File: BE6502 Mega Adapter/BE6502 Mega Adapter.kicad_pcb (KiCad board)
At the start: 2 copper layers, 99.1 x 99.1 mm, 12 parts, among them J1 Expansion, J2 Slot #1, J3 Slot #2, M1 Mounting, M2 Mounting, M3 Mounting, M4 Mounting

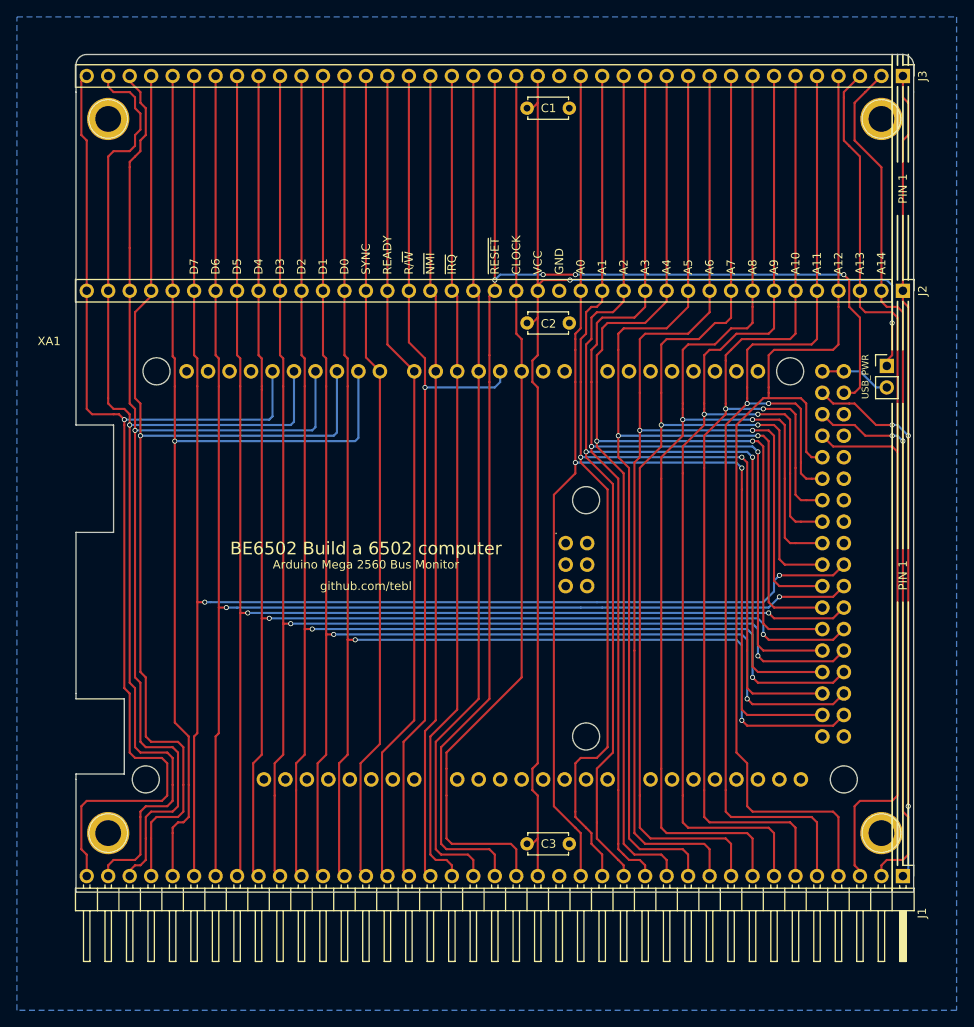
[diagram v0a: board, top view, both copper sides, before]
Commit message: Updated Mega shield silkscreen
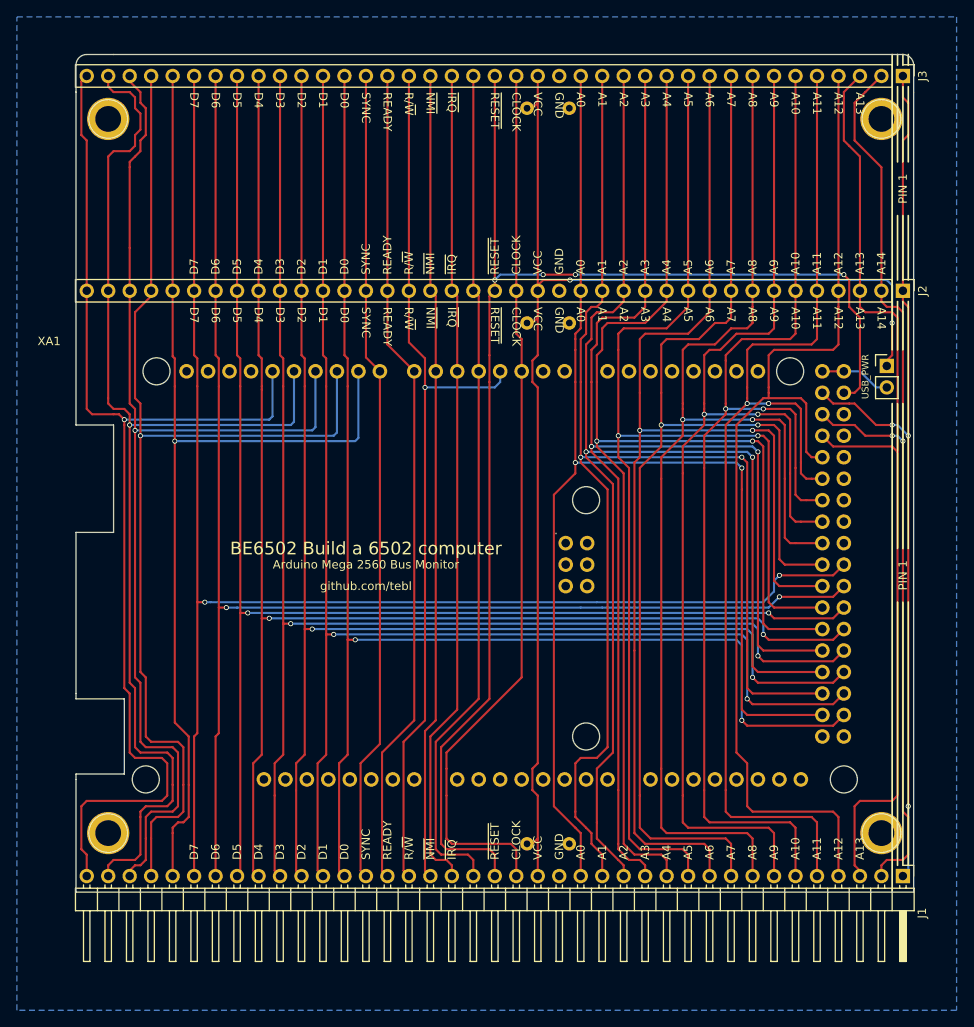
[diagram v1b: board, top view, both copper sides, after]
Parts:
- C1, C2, C3: moved to B.Cu
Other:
- board text added: "Link to power from/to Arduino"
